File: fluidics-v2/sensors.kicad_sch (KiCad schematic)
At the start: 21 parts, among them IC3 HSCDRRN001BDSA3, IC4 HSCDRRN001BDSA3, IC5 HSCDRRN001BDSA3, IC6 HSCDRRN001BDSA3, U12 LTC4316CMS-TRPBF

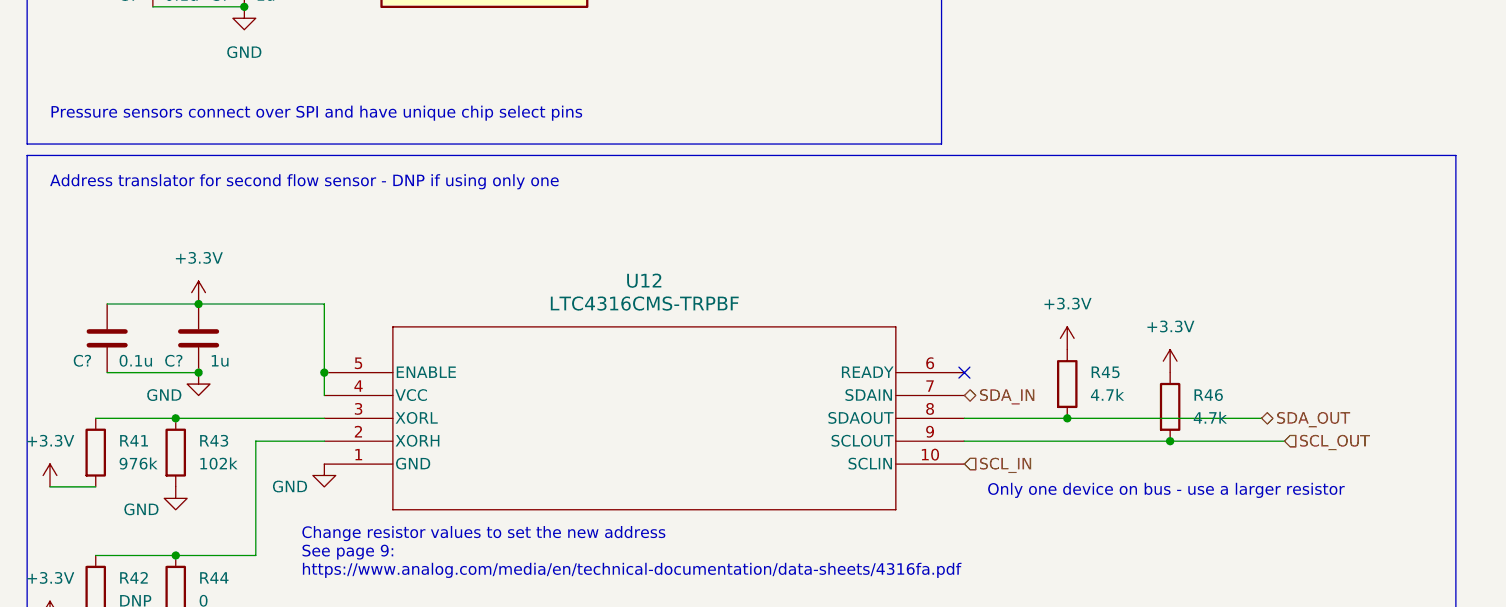
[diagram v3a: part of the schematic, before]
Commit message: added pressure controllers and more flow sensors
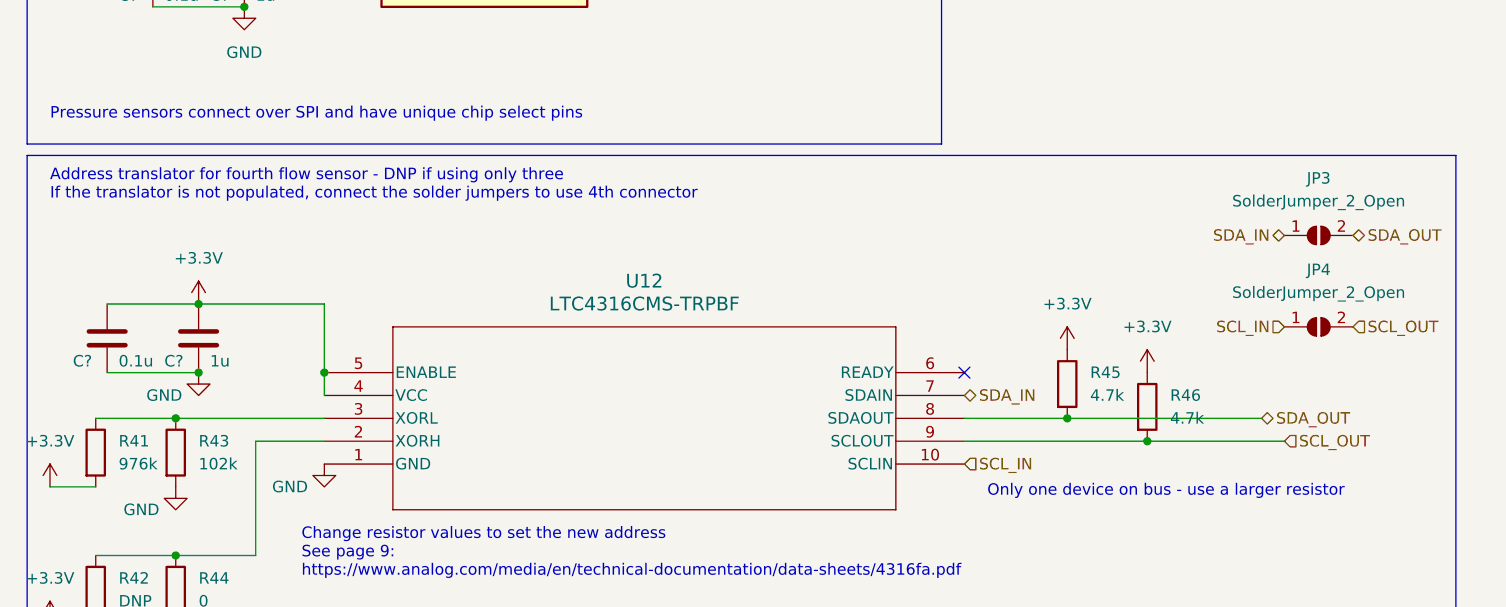
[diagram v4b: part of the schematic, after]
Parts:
- added JP3, JP4: SolderJumper_2_Open, Jumper:SolderJumper-2_P1.3mm_Open_TrianglePad1.0x1.5mm, symbol Jumper:SolderJumper_2_Open
- C? (x5): footprint Capacitor_SMD:C_0603_1608Metric -> Capacitor_SMD:C_0805_2012Metric
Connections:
- net SCL_IN: now also JP4.1 (A)
- net SCL_OUT: now also JP4.2 (B)
- net SDA_IN: now also JP3.1 (A)
- net SDA_OUT: now also JP3.2 (B)
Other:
- note added: "Address translator for fourth flow sensor - DNP if using only three If the translator is not populated, connect the solder jumpers to use 4th connector"
- note removed: "Address translator for second flow sensor - DNP if using only one"
- moved on the sheet: R46
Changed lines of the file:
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@@
   (junction (at 39.37 114.3) (diameter 0) (color 0 0 0 0)
   )
-  (junction (at 142.24 170.18) (diameter 0) (color 0 0 0 0)
-  )
   (junction (at 39.37 54.61) (diameter 0) (color 0 0 0 0)
   )
@@
   )
   (junction (at 34.29 154.94) (diameter 0) (color 0 0 0 0)
+  )
+  (junction (at 139.7 170.18) (diameter 0) (color 0 0 0 0)
   )
   (junction (at 31.75 182.88) (diameter 0) (color 0 0 0 0)
@@
     (stroke (width 0) (type default))
   )
-  (wire (pts (xy 119.38 170.18) (xy 142.24 170.18))
+  (wire (pts (xy 119.38 170.18) (xy 139.7 170.18))
     (stroke (width 0) (type default))
   )
@@
     (stroke (width 0) (type default))
   )
+  (wire (pts (xy 139.7 170.18) (xy 154.94 170.18))
+    (stroke (width 0) (type default))
+  )
   (wire (pts (xy 29.21 69.85) (xy 39.37 69.85))
     (stroke (width 0) (type default))
@@
   )
   (wire (pts (xy 130.81 167.64) (xy 152.4 167.64))
-    (stroke (width 0) (type default))
-  )
-  (wire (pts (xy 142.24 170.18) (xy 154.94 170.18))
     (stroke (width 0) (type default))
   )
@@
     (effects (font (size 1.27 1.27)) (justify left bottom))
   )
-  (text "Address translator for second flow sensor - DNP if using only one"
-    (at 17.78 142.24 0)
+  (text "Address translator for fourth flow sensor - DNP if using only three\nIf the translator is not populated, connect the solder jumpers to use 4th connector"
+    (at 17.78 143.51 0)
     (effects (font (size 1.27 1.27)) (justify left bottom))
   )
@@
     (effects (font (size 1.27 1.27)) (justify left bottom))
   )
+  (hierarchical_label "SDA_IN" (shape bidirectional) (at 154.94 147.32 180) (fields_autoplaced)
+    (effects (font (size 1.27 1.27)) (justify right))
+  )
+  (hierarchical_label "SCL_OUT" (shape input) (at 162.56 157.48 0) (fields_autoplaced)
+    (effects (font (size 1.27 1.27)) (justify left))
+  )
+  (hierarchical_label "SCL_IN" (shape input) (at 154.94 157.48 180) (fields_autoplaced)
+    (effects (font (size 1.27 1.27)) (justify right))
+  )
   (hierarchical_label "SCL_IN" (shape input) (at 119.38 172.72 0) (fields_autoplaced)
     (effects (font (size 1.27 1.27)) (justify left))
@@
   )
   (hierarchical_label "SDA_OUT" (shape bidirectional) (at 152.4 167.64 0) (fields_autoplaced)
+    (effects (font (size 1.27 1.27)) (justify left))
+  )
+  (hierarchical_label "SDA_OUT" (shape bidirectional) (at 162.56 147.32 0) (fields_autoplaced)
     (effects (font (size 1.27 1.27)) (justify left))
   )
@@
     )
   )
+  (symbol (lib_id "Jumper:SolderJumper_2_Open") (at 158.75 147.32 0) (unit 1)
+    (in_bom yes) (on_board yes) (dnp no) (fields_autoplaced)
+    (property "Reference" "JP3" (at 158.75 140.97 0)
+      (effects (font (size 1.27 1.27)))
+    )
+    (property "Value" "SolderJumper_2_Open" (at 158.75 143.51 0)
+      (effects (font (size 1.27 1.27)))
+    )
+    (property "Footprint" "Jumper:SolderJumper-2_P1.3mm_Open_TrianglePad1.0x1.5mm" (at 158.75 147.32 0)
+      (effects (font (size 1.27 1.27)) hide)
+    )
+    (property "Datasheet" "~" (at 158.75 147.32 0)
+      (effects (font (size 1.27 1.27)) hide)
+    )
+    (pin "1")
+    (pin "2")
+    (instances
+      (project "fluidics-v2"
+        (path "/0ec91c42-8aad-437d-8c85-5e10f0e51fe0/978ef52c-7a59-4000-92fc-4e58ca2b1aa7"
+          (reference "JP3") (unit 1)
+        )
+      )
+    )
+  )
   (symbol (lib_id "Device:R") (at 31.75 171.45 0) (unit 1)
     (in_bom yes) (on_board yes) (dnp no) (fields_autoplaced)
@@
       (effects (font (size 1.27 1.27)) (justify left))
     )
-    (property "Footprint" "Capacitor_SMD:C_0603_1608Metric" (at 40.3352 121.92 0)
+    (property "Footprint" "Capacitor_SMD:C_0805_2012Metric" (at 40.3352 121.92 0)
       (effects (font (size 1.27 1.27)) hide)
     )
@@
         (path "/0ec91c42-8aad-437d-8c85-5e10f0e51fe0/978ef52c-7a59-4000-92fc-4e58ca2b1aa7"
           (reference "#PWR0146") (unit 1)
+        )
+      )
+    )
+  )
+  (symbol (lib_id "Jumper:SolderJumper_2_Open") (at 158.75 157.48 0) (unit 1)
+    (in_bom yes) (on_board yes) (dnp no) (fields_autoplaced)
+    (property "Reference" "JP4" (at 158.75 151.13 0)
+      (effects (font (size 1.27 1.27)))
+    )
+    (property "Value" "SolderJumper_2_Open" (at 158.75 153.67 0)
+      (effects (font (size 1.27 1.27)))
+    )
+    (property "Footprint" "Jumper:SolderJumper-2_P1.3mm_Open_TrianglePad1.0x1.5mm" (at 158.75 157.48 0)
+      (effects (font (size 1.27 1.27)) hide)
+    )
+    (property "Datasheet" "~" (at 158.75 157.48 0)
+      (effects (font (size 1.27 1.27)) hide)
+    )
+    (pin "1")
+    (pin "2")
+    (instances
+      (project "fluidics-v2"
+        (path "/0ec91c42-8aad-437d-8c85-5e10f0e51fe0/978ef52c-7a59-4000-92fc-4e58ca2b1aa7"
+          (reference "JP4") (unit 1)
         )
       )
@@
     )
   )
-  (symbol (lib_id "power:+3.3V") (at 142.24 162.56 0) (unit 1)
-    (in_bom yes) (on_board yes) (dnp no) (fields_autoplaced)
-    (property "Reference" "#PWR0150" (at 142.24 166.37 0)
-      (effects (font (size 1.27 1.27)) hide)
-    )
-    (property "Value" "+3.3V" (at 142.24 157.48 0)
-      (effects (font (size 1.27 1.27)))
-    )
-    (property "Footprint" "" (at 142.24 162.56 0)
-      (effects (font (size 1.27 1.27)) hide)
-    )
-    (property "Datasheet" "" (at 142.24 162.56 0)
+  (symbol (lib_id "power:+3.3V") (at 139.7 162.56 0) (unit 1)
+    (in_bom yes) (on_board yes) (dnp no) (fields_autoplaced)
+    (property "Reference" "#PWR0150" (at 139.7 166.37 0)
+      (effects (font (size 1.27 1.27)) hide)
+    )
+    (property "Value" "+3.3V" (at 139.7 157.48 0)
+      (effects (font (size 1.27 1.27)))
+    )
+    (property "Footprint" "" (at 139.7 162.56 0)
+      (effects (font (size 1.27 1.27)) hide)
+    )
+    (property "Datasheet" "" (at 139.7 162.56 0)
       (effects (font (size 1.27 1.27)) hide)
     )
@@
       (effects (font (size 1.27 1.27)) (justify left))
     )
-    (property "Footprint" "Capacitor_SMD:C_0603_1608Metric" (at 40.3352 54.61 0)
+    (property "Footprint" "Capacitor_SMD:C_0805_2012Metric" (at 40.3352 54.61 0)
       (effects (font (size 1.27 1.27)) hide)
     )
@@
       (effects (font (size 1.27 1.27)) (justify left))
     )
-    (property "Footprint" "Capacitor_SMD:C_0603_1608Metric" (at 35.2552 162.56 0)
+    (property "Footprint" "Capacitor_SMD:C_0805_2012Metric" (at 35.2552 162.56 0)
       (effects (font (size 1.27 1.27)) hide)
     )
@@
     )
   )
-  (symbol (lib_id "Device:R") (at 142.24 166.37 0) (unit 1)
-    (in_bom yes) (on_board yes) (dnp no) (fields_autoplaced)
-    (property "Reference" "R46" (at 144.78 165.1 0)
-      (effects (font (size 1.27 1.27)) (justify left))
-    )
-    (property "Value" "4.7k" (at 144.78 167.64 0)
-      (effects (font (size 1.27 1.27)) (justify left))
-    )
-    (property "Footprint" "Resistor_SMD:R_0402_1005Metric" (at 140.462 166.37 90)
-      (effects (font (size 1.27 1.27)) hide)
-    )
-    (property "Datasheet" "~" (at 142.24 166.37 0)
+  (symbol (lib_id "Device:R") (at 139.7 166.37 0) (unit 1)
+    (in_bom yes) (on_board yes) (dnp no) (fields_autoplaced)
+    (property "Reference" "R46" (at 142.24 165.1 0)
+      (effects (font (size 1.27 1.27)) (justify left))
+    )
+    (property "Value" "4.7k" (at 142.24 167.64 0)
+      (effects (font (size 1.27 1.27)) (justify left))
+    )
+    (property "Footprint" "Resistor_SMD:R_0402_1005Metric" (at 137.922 166.37 90)
+      (effects (font (size 1.27 1.27)) hide)
+    )
+    (property "Datasheet" "~" (at 139.7 166.37 0)
       (effects (font (size 1.27 1.27)) hide)
     )
@@
       (effects (font (size 1.27 1.27)) (justify left))
     )
-    (property "Footprint" "Capacitor_SMD:C_0603_1608Metric" (at 40.3352 77.47 0)
+    (property "Footprint" "Capacitor_SMD:C_0805_2012Metric" (at 40.3352 77.47 0)
       (effects (font (size 1.27 1.27)) hide)
     )
@@
       (effects (font (size 1.27 1.27)) (justify left))
     )
-    (property "Footprint" "Capacitor_SMD:C_0603_1608Metric" (at 40.3352 99.06 0)
-      (effects (font (size 1.27 1.27)) hide)
-    )
+    (property "Footprint" "Capacitor_SMD:C_0805_2012Metric" (at 40.3352 99.06 0)
+      (effects (font (size 1.27 1.27)) hide)
+    )

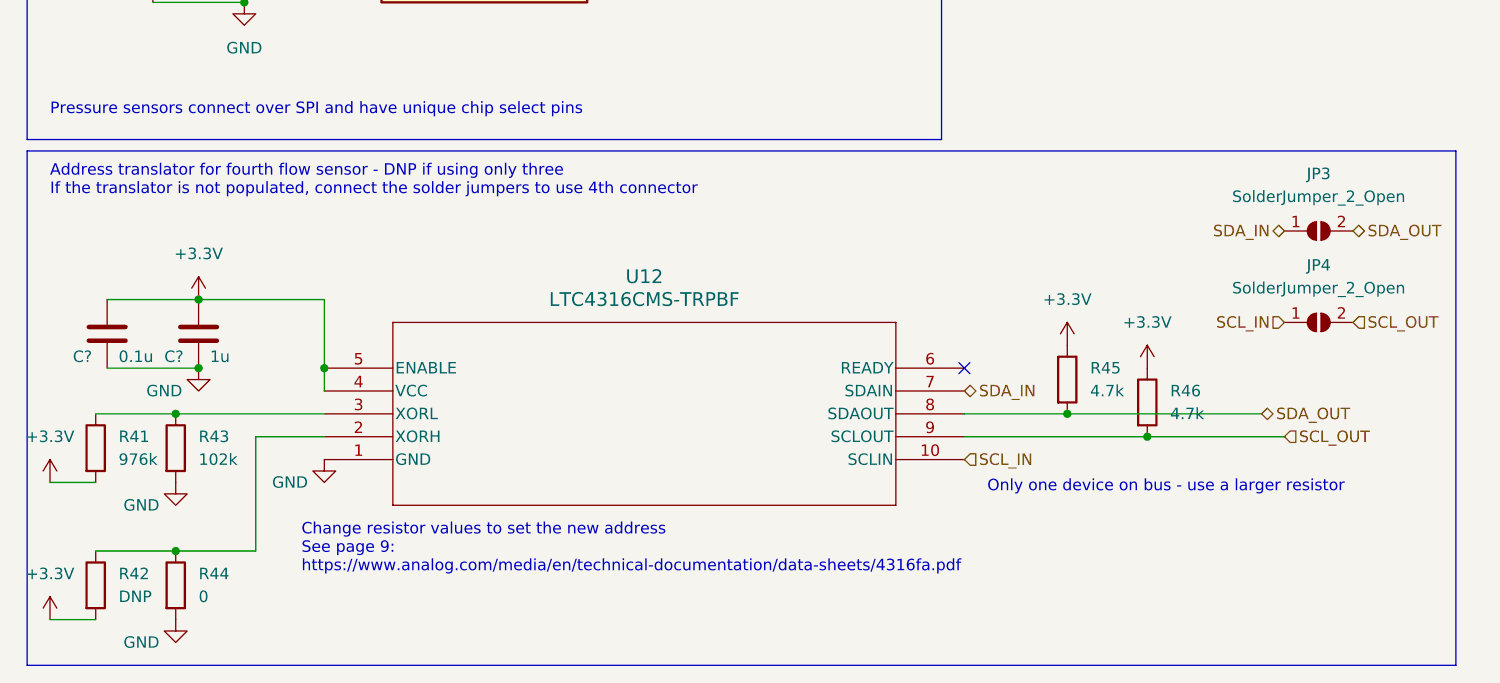
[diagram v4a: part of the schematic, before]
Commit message: added new connector for motor control daughter board. began layout
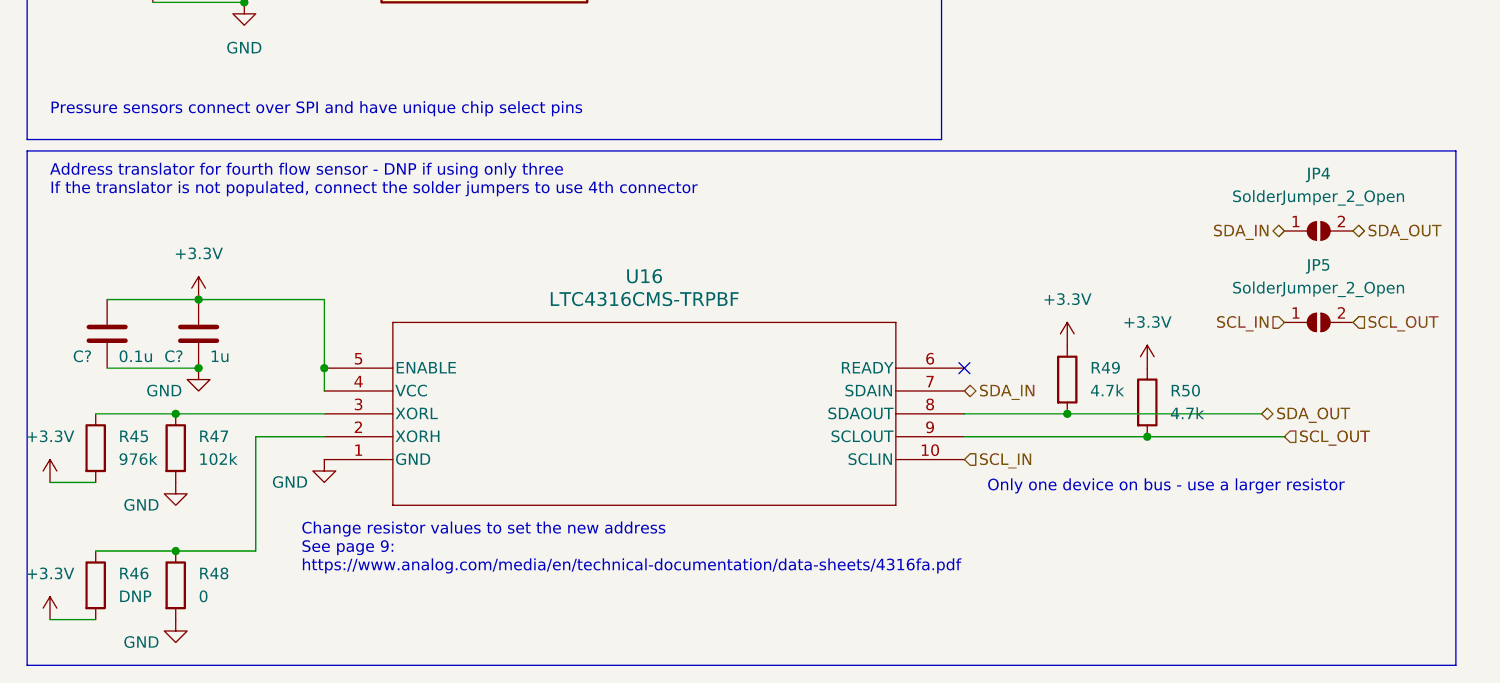
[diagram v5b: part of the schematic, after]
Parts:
- renumbered JP3 to JP4, JP4 to JP5, R41 to R45, R42 to R46, R43 to R47, R44 to R48, R45 to R49, R46 to R50, U12 to U16

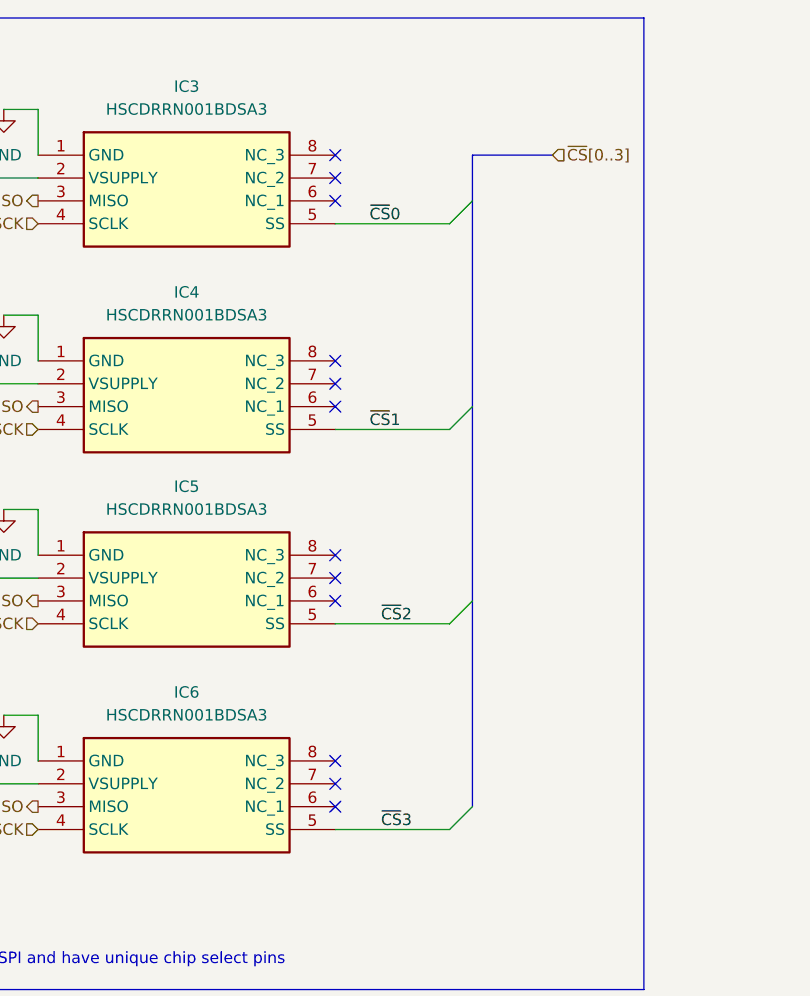
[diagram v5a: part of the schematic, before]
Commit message: added pullups/downs to spi for stability, rounded corners
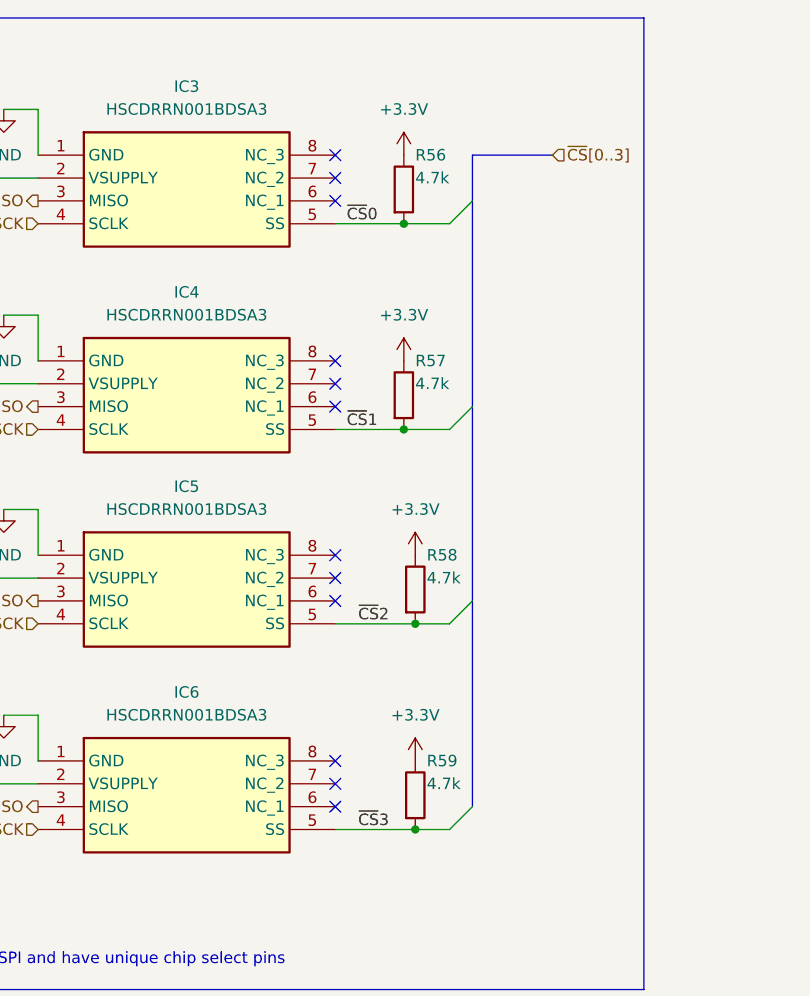
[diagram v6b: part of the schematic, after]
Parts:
- added R56, R57, R58, R59: 4.7k, Resistor_SMD:R_0402_1005Metric, symbol Device:R
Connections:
- net +3.3V: now also R56.1, R57.1, R58.1, R59.1
- net ~{CS}0: now also R56.2
- net ~{CS}1: now also R57.2
- net ~{CS}2: now also R58.2
- net ~{CS}3: now also R59.2
